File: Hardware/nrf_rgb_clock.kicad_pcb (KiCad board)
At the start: 4 copper layers, 230 x 230 mm, 220 parts, among them J1 Conn_01x02, J3 Conn_01x07_Pin, U1 AMS1117-3.3, U3 TPS54260DGQ, Y1 32MHz

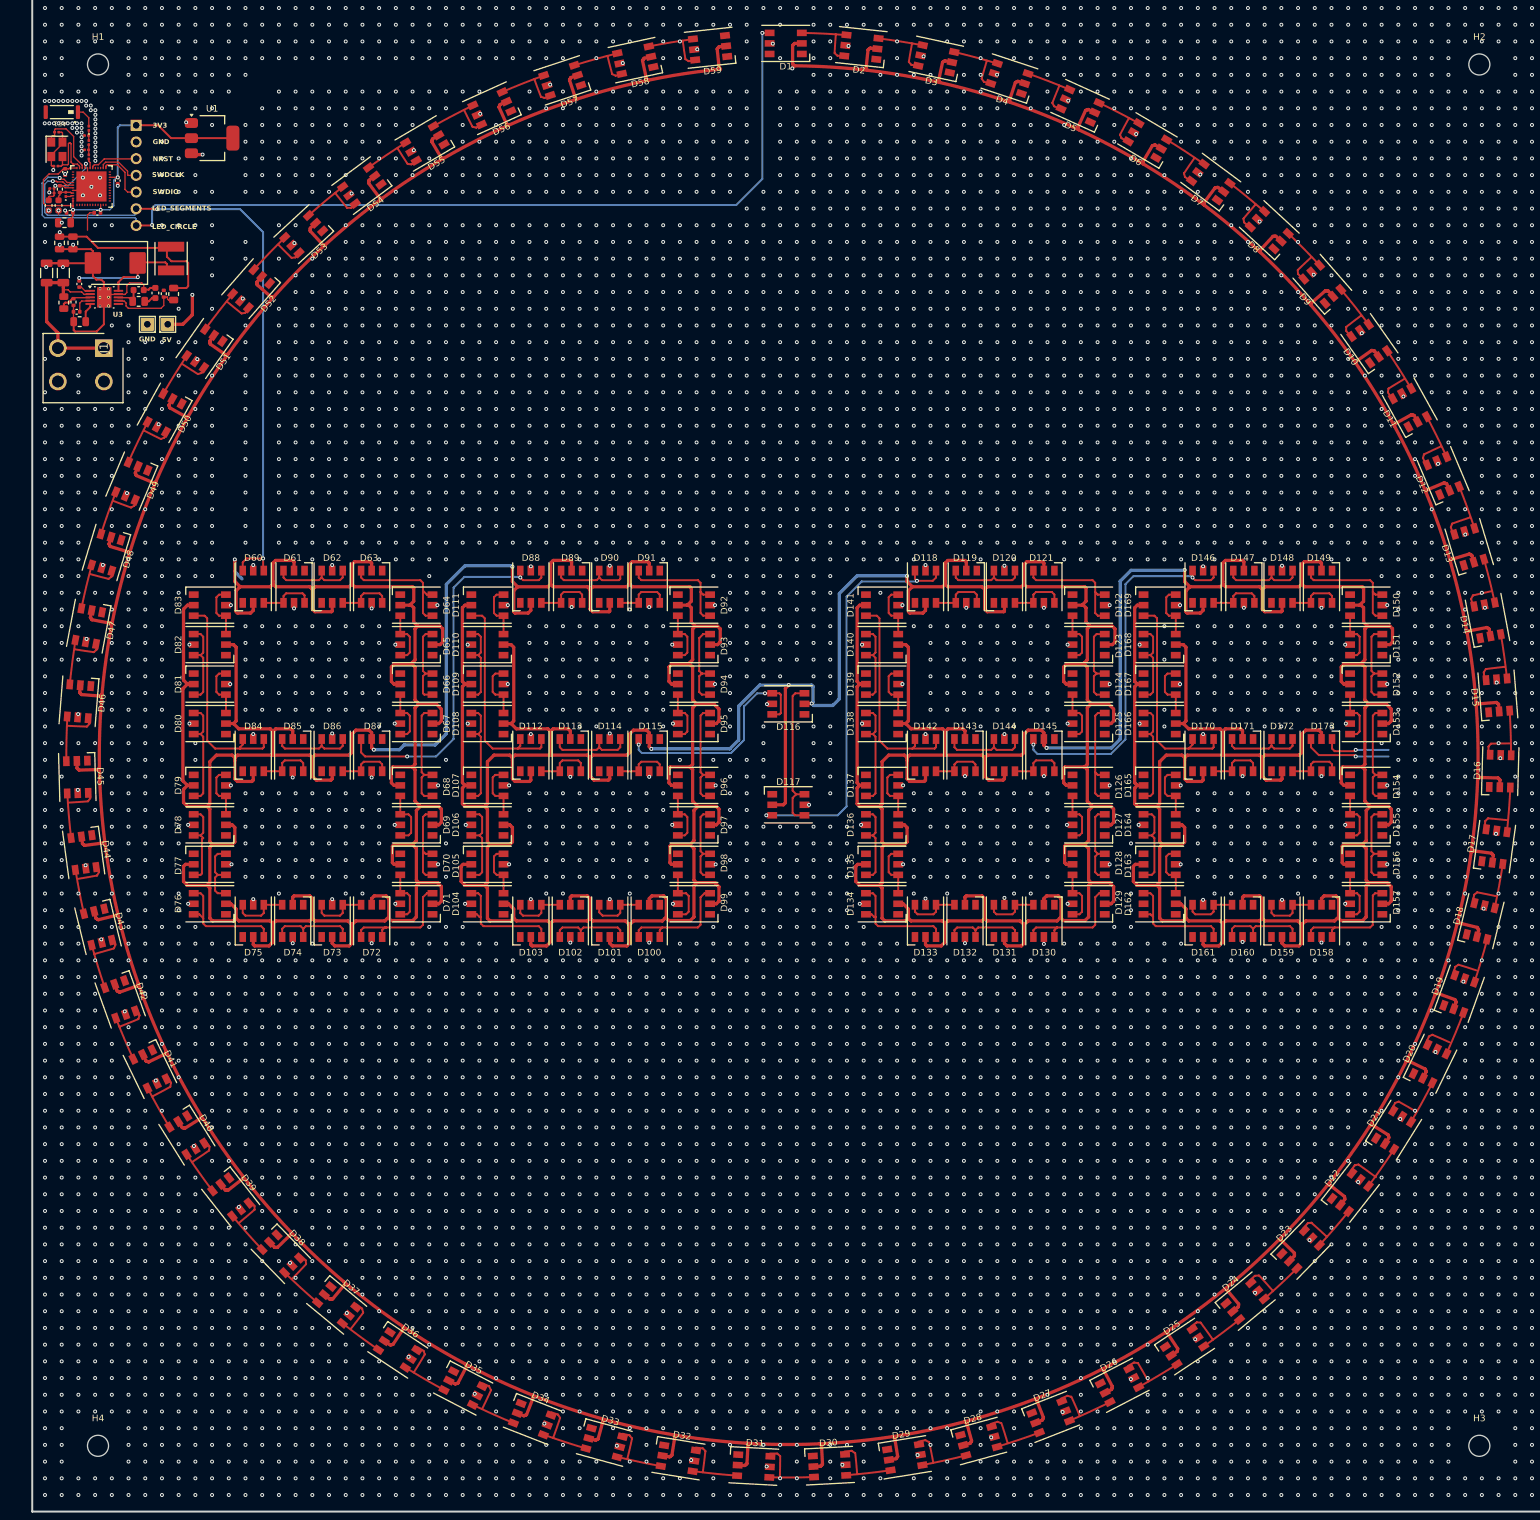
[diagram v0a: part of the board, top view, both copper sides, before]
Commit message: finalized layout, via stitching
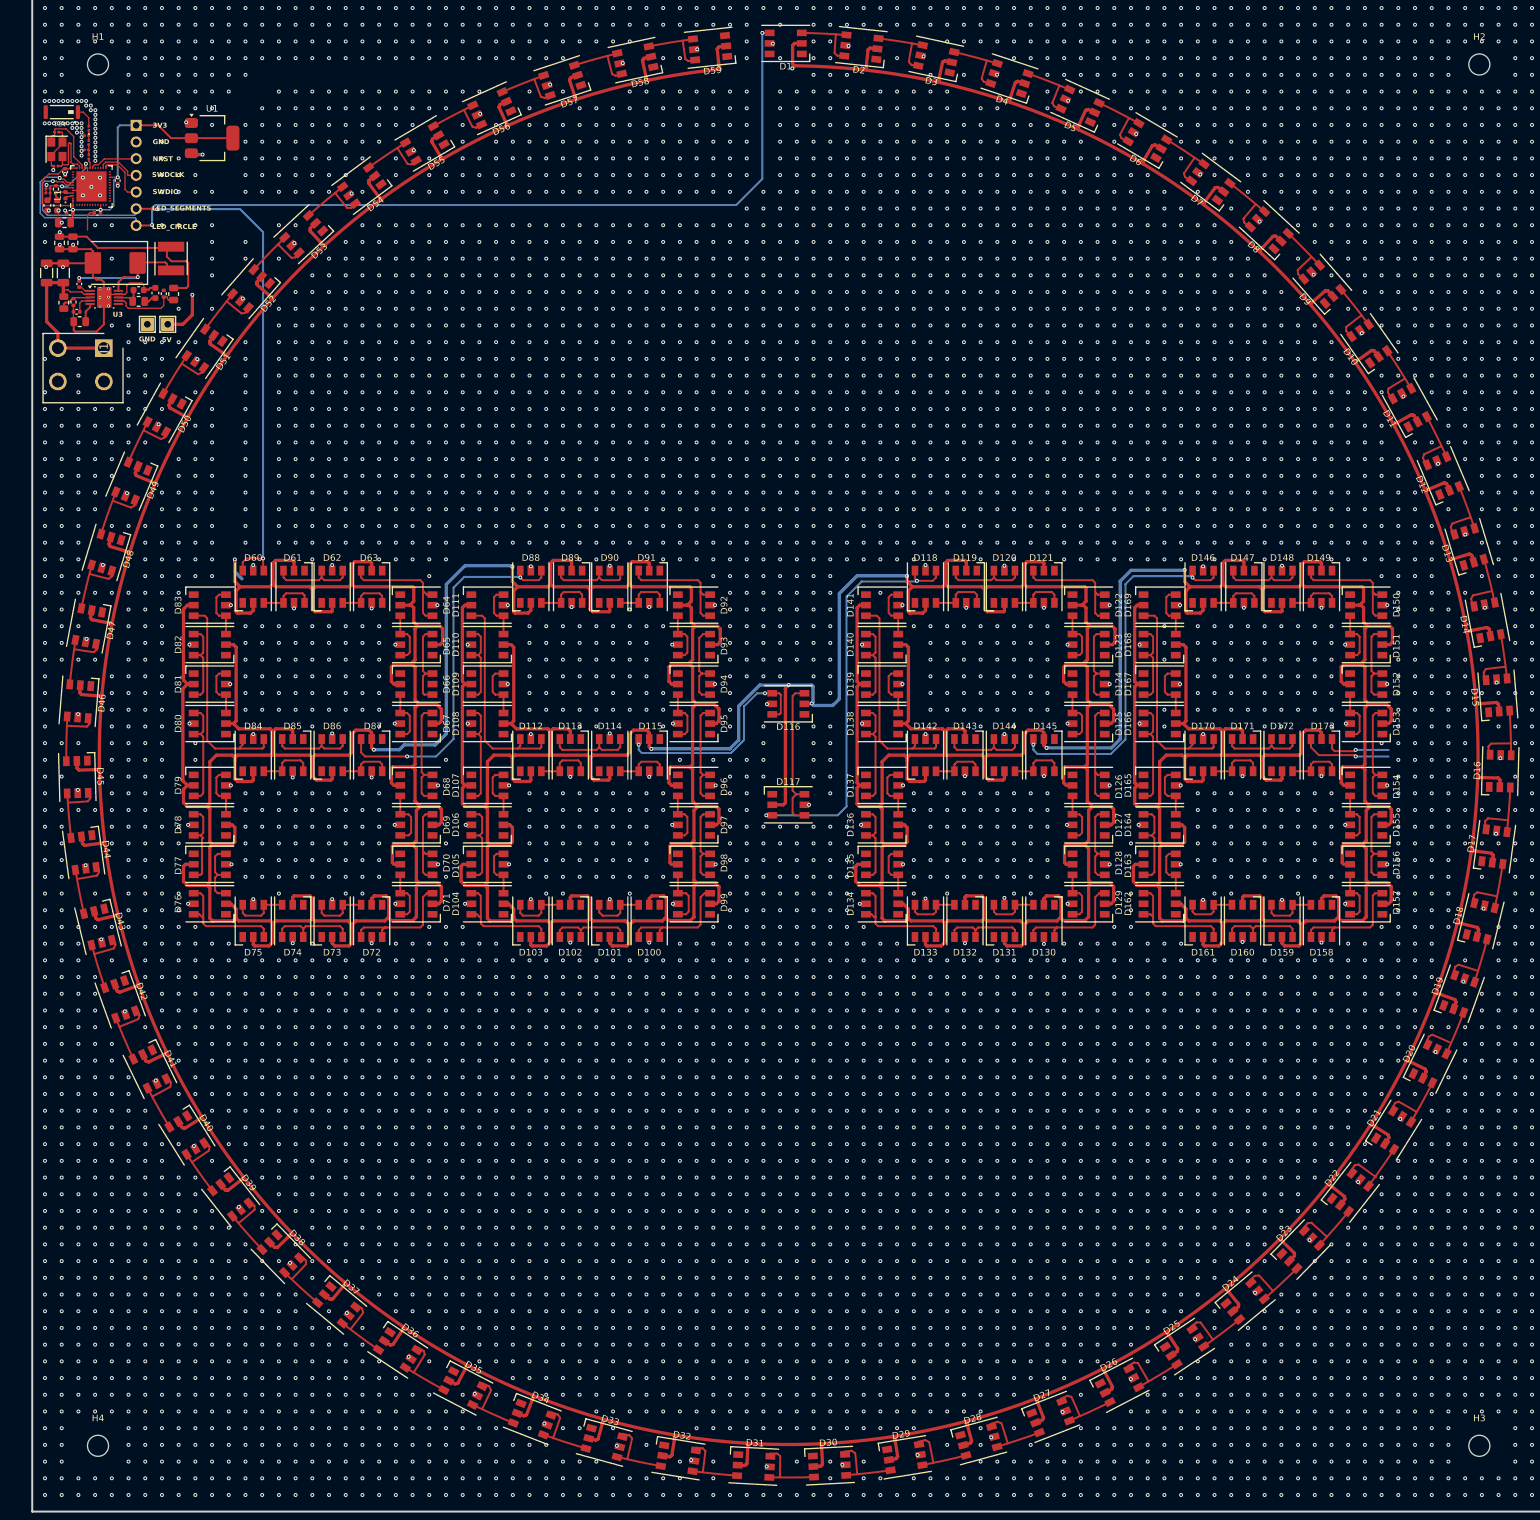
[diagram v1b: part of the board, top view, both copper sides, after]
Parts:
- L1: footprint LED_SMD:LED_0201_0603Metric -> LED_SMD:LED_0402_1005Metric
- moved C6 0.60 mm to (227.4, 134.1)
- moved C7 0.60 mm to (227.4, 134.8)
- moved FB1 0.60 mm to (228.6, 134.2)
- moved C4 0.20 mm to (228.8, 136.6)
- moved C5 0.20 mm to (227.3, 136.6)
- moved L1 0.14 mm to (230.1, 135.1)
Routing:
- net Net-(U4-DECA): track 13.0 -> 12.1 mm
- net Net-(U4-DECD): track 3.33 -> 3.97 mm
- net LED_SEGMENTS: track 100.9 -> 101.5 mm
- net LED_CIRCLE: track 148.9 -> 149.4 mm
- net GND: track 156.4 -> 156.9 mm, vias 6560 -> 6414

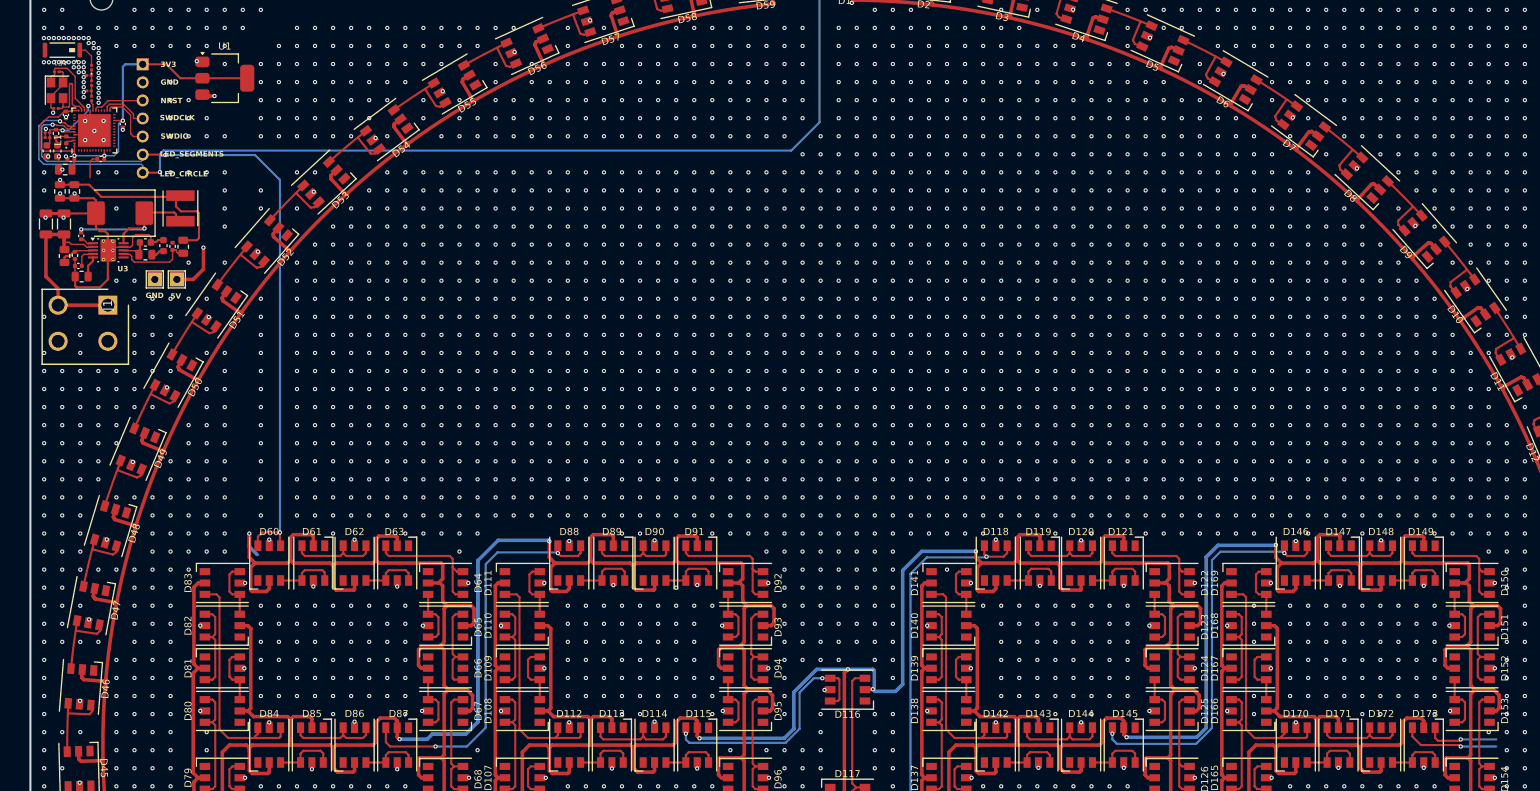
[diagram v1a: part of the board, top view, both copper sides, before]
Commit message: changed antenna
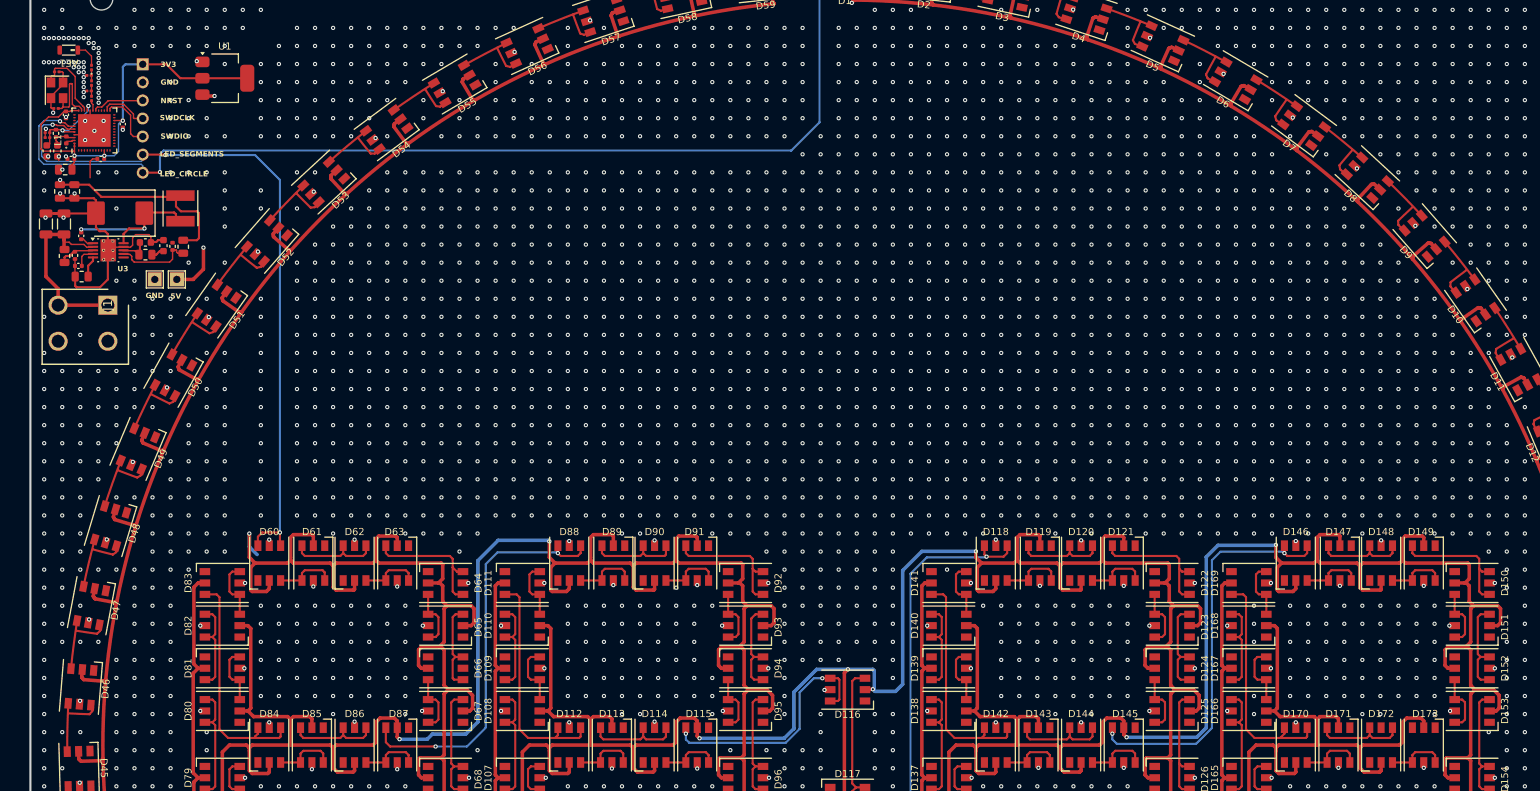
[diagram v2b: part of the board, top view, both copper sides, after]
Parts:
- AE1: footprint ProjectFootprints:2450AT43A100E -> ProjectFootprints:2450AT18A100
- C17, C18: value ?p -> 18p
- moved AE1 0.90 mm to (230.4, 122.4)
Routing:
- net /led_segment3/LED_DO: track 13.6 -> 0.00 mm, vias 1 -> 0
- net unconnected-(D173-VCC-Pad1): track 10.3 -> 0.00 mm, vias 1 -> 0

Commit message: removed d* reference designators
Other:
- board text added: "nrf_rgb_clock v 1.0 by Ihysol 12th march 2025"
